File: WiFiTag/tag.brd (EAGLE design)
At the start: 46 x 36 mm, 65 parts, among them IC2 MCP73831/OT, U2 CP2104-F03-GM

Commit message: WifiTagV0.4
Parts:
- removed C4: 10uF, microbuilder:0603
- removed D2: (no value), adafruit:SOD-123
- removed EN, VBUS: (no value), wirepad:SMD1,27-2,54
- removed LED2: RED, microbuilder:CHIPLED_0603
- removed LED3: GREEN, microbuilder:CHIPLED_0603
- removed R8, R9: 10k, microbuilder:0402
- removed T1, T2: (no value), transistor:SOT23-BEC
- removed U2: CP2104-F03-GM, Silicon Labs:QFN-24-4X4
- removed U3: (no value), MicroUSB:USB-MICRO-SMD
- added GND1, SET: (no value), wirepad:SMD1,27-2,54
- added JP1, JP2: (no value), pinhead:1_05X2MM
- R4, R5: value 1k -> 10k
- moved R5 31.8 mm to (35.0, 8.00), turned to 180 degrees
- moved R4 28.4 mm to (31.0, 8.00), turned to 0 degrees
- moved C3 2.00 mm to (14.0, 18.0)
- moved C2 1.00 mm to (19.0, 27.0)
- moved C5 1.00 mm to (21.0, 27.0)
- moved R12 1.00 mm to (24.0, 29.0)
- moved U1 1.00 mm to (16.0, 27.0)
- moved R7 0.26 mm to (27.0, 8.00)
- turned R2 to 90 degrees
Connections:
- removed net D+: U2.3, U3.D+1
- removed net D-: U2.4, U3.D-1
- removed net DTR: R8.1, T2.E, U2.23
- removed net N$10: R8.2, T1.B
- removed net N$11: R9.2, T2.B
- removed net N$6: LED2.A, R4.2
- removed net N$7: LED3.A, R5.2
- removed net N$8: LED2.C, U2.14
- removed net N$9: LED3.C, U2.13
- removed net RTS: R9.1, T1.E, U2.19
- removed net VBUS: C4.1, D2.A, U2.7, U2.8, U3.VBUS1, VBUS.1
- net 0: now also JP1.1, R4.1; no longer R18.1, T2.C
- net 2: now also R18.1
- net 3.3V: now also JP2.4, R4.2, R5.2, U$24.EN
- net 5.0V: now also JP2.5; no longer D2.C
- net EN: now also JP1.5; no longer EN.1
- net GND: now also GND1.1, JP2.1; no longer C4.2, U2.2, U2.PAD, U3.GND1
- net RST: now also JP1.2, R5.1; no longer T1.C
- net RXD: now also JP1.3; no longer U2.20
- net SETLATCH: now also SET.1; no longer R4.1, R5.1, U2.5, U2.6
- net TXD: now also JP1.4; no longer U2.21
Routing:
- net DTR: track 28.5 -> 0.00 mm
- net RTS: track 28.1 -> 0.00 mm
- net 3.3V: track 62.2 -> 89.8 mm, vias 0 -> 3
- net 2: track 2.60 -> 28.2 mm, vias 0 -> 2
- net EN: track 20.0 -> 41.2 mm
- net RST: track 45.8 -> 66.0 mm
- net VBUS: track 17.4 -> 0.00 mm
- net 0: track 28.8 -> 45.1 mm, vias 2 -> 1
- net D+: track 13.0 -> 0.00 mm
- net SETLATCH: track 42.8 -> 31.3 mm, vias 5 -> 3
- net D-: track 11.5 -> 0.00 mm
- net TXD: track 44.5 -> 34.4 mm, vias 2 -> 1
- net RXD: track 45.2 -> 37.7 mm, vias 2 -> 1
- net N$10: track 4.85 -> 0.00 mm
- net 5.0V: track 40.8 -> 45.3 mm, vias 0 -> 1
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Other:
- outline, holes or cut-outs redrawn
- board text added: "V0.4"
- board text removed: "V0.3"

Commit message: new tag version 0.5
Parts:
- removed JP1, JP2: (no value), pinhead:1_05X2MM
- removed U$21, U$47, U$48, U$49: MOUNTINGHOLE2.5, microbuilder:MOUNTINGHOLE_2.5_PLATED
- removed U$24: CD4043B, masterthesis:TSSOP16
- added 16, BAT1, EN: (no value), wirepad:SMD1,27-2,54
- added Q1: (no value), microbuilder:SOT23-R
- added R8: 10k, microbuilder:0402
- R20: value 150 -> 10k
- moved SET 49.4 mm to (2.00, 3.00)
- moved GND1 41.2 mm to (4.00, 18.0)
- moved 3.3V 27.9 mm to (2.00, 27.0), turned to 90 degrees
- moved U5 23.4 mm to (33.8, 4.10), turned to 180 degrees
- moved R5 22.5 mm to (43.0, 29.0), turned to 90 degrees
- moved U4 9.09 mm to (38.0, 29.0), turned to 270 degrees
- moved 5V 9.06 mm to (2.00, 33.0), turned to 90 degrees
- moved R19 7.07 mm to (34.0, 33.0), turned to 270 degrees
- moved LED1 7.00 mm to (15.0, 33.0)
- moved LED6 7.00 mm to (15.0, 3.00)
- moved R1 7.00 mm to (13.0, 33.0)
- moved R18 7.00 mm to (13.0, 3.00), turned to 90 degrees
- moved AC1 5.00 mm to (29.0, 4.00)
- moved AC2 5.00 mm to (27.0, 4.00)
- moved BAT 5.00 mm to (27.0, 32.0)
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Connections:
- removed net BATLOW: R10.1, U$24.Q2
- removed net RESETLATCH: U$24.R1, U4.4
- removed net SETLATCH: SET.1, U$24.S1, U5.11
- new net N$6: Q1.3, R8.2, U4.2
- new net SET: Q1.2, SET.1, U5.11
- net 0: no longer JP1.1
- net 12: no longer U$24.S2
- net 14: now also R10.1; no longer U$24.R2
- net 16: now also 16.1, Q1.1; no longer U4.2
- net 2: now also LED6.C; no longer R18.1
- net 3.3V: now also R18.2, U5.8; no longer JP2.4, U$24.EN, U$24.VCC
- net 4.5V: now also BAT1.1
- net 5.0V: no longer JP2.5
- net EN: now also EN.1, U4.4; no longer JP1.5, U$24.Q1
- net GND: now also R8.1, U5.12; no longer JP2.1, LED6.C, U$24.GND
- net N$4: now also R18.1; no longer R18.2
- net RST: no longer JP1.2
- net RXD: no longer JP1.3
- net TXD: no longer JP1.4
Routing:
- net SET: track 0.00 -> 59.1 mm, vias 0 -> 2
- net 0: track 45.1 -> 2.51 mm, vias 1 -> 0
- net RST: track 66.0 -> 24.2 mm, vias 2 -> 0
- net RXD: track 37.7 -> 0.00 mm, vias 1 -> 0
- net TXD: track 34.4 -> 0.00 mm, vias 1 -> 0
- net 16: track 14.6 -> 47.0 mm
- net SETLATCH: track 31.3 -> 0.00 mm, vias 3 -> 0
- net 4.5V: track 13.2 -> 39.2 mm, vias 0 -> 2
- net 12: track 16.3 -> 0.00 mm
- net 4: track 17.9 -> 5.26 mm, vias 2 -> 0
- net 5.0V: track 45.3 -> 56.5 mm, vias 1 -> 0
- net 2: track 28.2 -> 19.0 mm
- net 3.3V: track 89.8 -> 98.2 mm, vias 3 -> 7
- net 14: track 13.0 -> 20.3 mm
- net N$6: track 0.00 -> 6.29 mm
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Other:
- outline, holes or cut-outs redrawn
- board text added: "V0.5"
- board text removed: "V0.4"

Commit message: XNOR Tag version
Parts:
- removed Q1: (no value), microbuilder:SOT23-R
- removed R8: 10k, microbuilder:0402
- removed U4: (no value), microbuilder:SOT23-5
- added C14: 470nF, microbuilder:0402
- added C4: 10nF, microbuilder:0402
- added R21, R22, R23, R9: 10k, microbuilder:0402
- added R24, R25: 100k, microbuilder:0402
- added U$46: CD4077B, masterthesis:TSSOP14
- R1: value (none) -> 1k
- moved R20 10.3 mm to (31.0, 31.5), turned to 90 degrees
- moved R19 10.3 mm to (43.0, 28.0), turned to 90 degrees
- moved R13 2.70 mm to (29.0, 28.5)
- moved U5 2.41 mm to (36.0, 5.00)
- moved R5 2.24 mm to (41.0, 28.0)
- moved R12 2.06 mm to (27.0, 28.5), turned to 90 degrees
- moved 3.3V 1.00 mm to (2.00, 28.0)
- moved C1 1.00 mm to (24.2, 32.2)
- moved D1 1.00 mm to (23.0, 29.0)
- moved IC2 1.00 mm to (21.0, 32.0)
- moved R2 1.00 mm to (18.0, 32.0)
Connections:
- removed net N$6: Q1.3, R8.2, U4.2
- new net N$10: R25.1, U$46.A
- new net N$7: R9.1, U5.7
- new net N$8: R21.2, U5.8
- new net N$9: R20.2, U$46.~G#H
- net 12: now also R11.1
- net 13: no longer R11.1
- net 16: now also U$46.B, U$46.G; no longer Q1.1
- net 3.3V: now also C14.1, C4.2, R21.1, R22.2, R23.1, R24.2, R25.2, U$46.VCC; no longer R20.1, U4.5, U5.8
- net 4: now also R22.1
- net 5: now also R23.2
- net EN: now also R20.1, R24.1, U$46.~A#B; no longer R20.2, U4.4
- net GND: now also C14.2, C4.1, R9.2, U$46.GND; no longer R8.1, U4.3
- net SET: now also U$46.H; no longer Q1.2
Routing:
- net 13: track 35.6 -> 0.00 mm
- net 12: track 0.00 -> 32.4 mm
- net RST: track 24.2 -> 6.47 mm
- net 3.3V: track 98.2 -> 113.8 mm, vias 7 -> 9
- net 16: track 47.0 -> 55.5 mm, vias 2 -> 4
- net EN: track 47.5 -> 54.1 mm, vias 2 -> 6
- net N$6: track 6.29 -> 0.00 mm
- net N$10: track 0.00 -> 5.00 mm, vias 0 -> 2
- net SET: track 59.1 -> 63.9 mm
- net N$7: track 0.00 -> 4.59 mm, vias 0 -> 2
- net N$9: track 0.00 -> 3.90 mm
- net 14: track 20.3 -> 23.0 mm, vias 0 -> 2
- net 5: track 13.1 -> 15.7 mm
- net 4: track 5.26 -> 7.55 mm
- net 5.0V: track 56.5 -> 58.4 mm
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
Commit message: XNOR Tag version
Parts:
- removed AC1, AC2, BAT1, GND1: (no value), wirepad:SMD1,27-2,54
- removed C14: 470nF, microbuilder:0402
- removed C4: 10nF, microbuilder:0402
- removed R21, R22, R9: 10k, microbuilder:0402
- removed U5: (no value), microbuilder:LGA16_3X3MM
- added C17: 1uF, microbuilder:0402
- added C18: 100nf, microbuilder:0402
- added JP1, JP2: (no value), microbuilder:1X02_OVAL
- added Q3, Q4: BSS138, microbuilder:SOT23-WIDE
- added R31, R33, R34, R35, R36: 10K, microbuilder:0402
- added U3: LIS3DHTR, microbuilder:LGA16_3X3MM
- R32: value 10k -> 10K
- moved R11 32.2 mm to (17.0, 22.0)
- moved GND 28.7 mm to (4.00, 18.0), turned to 90 degrees
- moved BAT 26.9 mm to (2.00, 22.0), turned to 90 degrees
- moved R7 16.6 mm to (20.0, 23.0)
- moved R6 13.6 mm to (20.0, 21.0)
- moved R4 2.00 mm to (28.0, 8.00), turned to 180 degrees
- moved C3 1.00 mm to (14.0, 22.0)
- moved R3 1.00 mm to (14.0, 24.0)
- moved U1 1.00 mm to (14.0, 27.0)
- turned R32 to 270 degrees
- renumbered R23 to R32
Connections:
- removed net 4: R22.1, U5.6, X1.14
- removed net 5: R32.2, U5.4, X1.13
- removed net N$7: R9.1, U5.7
- removed net N$8: R21.2, U5.8
- new net ADC1: U3.16
- new net ADC2: U3.15
- new net ADC3: U3.13
- new net N$11: R31.1, U3.8
- new net SCL: Q4.3, R35.1, X1.13
- new net SCL_3.3V: Q4.2, R33.1, U3.4
- new net SDA: Q3.3, R34.1, X1.14
- new net SDA_3.3V: Q3.2, R32.1, U3.6
- new net SDO: R36.2, U3.7
- net 3.3V: now also C17.1, C18.1, Q3.1, Q4.1, R31.2, R32.2, R33.2, R34.2, R35.2, U3.1, U3.14; no longer C14.1, C4.2, R21.1, R22.2, R32.1, U5.1, U5.14
- net 4.5V: now also JP1.1; no longer BAT1.1
- net AC1: now also JP2.1; no longer AC1.1
- net AC2: now also JP2.2; no longer AC2.1
- net GND: now also C17.2, C18.2, JP1.2, R36.1, U3.10, U3.12, U3.5; no longer C14.2, C4.1, GND1.1, R9.2, U5.10, U5.12, U5.5
- net SET: now also U3.11; no longer U5.11
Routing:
- net N$13: track 2.04 -> 43.5 mm, vias 0 -> 2
- net 12: track 32.4 -> 12.3 mm, vias 0 -> 2
- net 5: track 15.7 -> 0.00 mm
- net 2: track 19.0 -> 32.3 mm
- net SDA_3.3V: track 0.00 -> 11.1 mm, vias 0 -> 2
- net SET: track 63.9 -> 74.5 mm, vias 2 -> 3
- net SDA: track 0.00 -> 10.0 mm
- net SDO: track 0.00 -> 8.15 mm
- net 4: track 7.55 -> 0.00 mm
- net SCL_3.3V: track 0.00 -> 7.54 mm, vias 0 -> 2
- net SCL: track 0.00 -> 6.43 mm
- net N$11: track 0.00 -> 5.53 mm
- net N$7: track 4.59 -> 0.00 mm, vias 2 -> 0
- net 3.3V: track 113.8 -> 117.6 mm, vias 9 -> 6
- net N$10: track 5.00 -> 7.50 mm
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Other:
- board text added: "V0.6"
- board text removed: "V0.5"

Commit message: V06 of PCB
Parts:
- removed R20: 10k, microbuilder:0402
- removed R25: 100k, microbuilder:0402
- removed U$46: CD4077B, masterthesis:TSSOP14
- added U2: (no value), microbuilder:SOT23-5
- R24: value 100k -> 10k
- moved R19 12.0 mm to (31.0, 28.5), turned to 270 degrees
- moved R5 6.02 mm to (35.0, 28.5)
- moved R24 2.00 mm to (33.0, 28.5), turned to 90 degrees
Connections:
- removed net N$10: R25.1, U$46.A
- removed net N$9: R20.2, U$46.~G#H
- net 16: no longer U$46.B, U$46.G
- net 3.3V: now also U2.5; no longer R25.2, U$46.VCC
- net EN: no longer R20.1, U$46.~A#B
- net GND: now also U2.3; no longer U$46.GND
- net RST: now also U2.4
- net SET: now also U2.2; no longer U$46.H
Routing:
- net EN: track 54.4 -> 41.4 mm, vias 6 -> 2
- net 16: track 55.5 -> 42.6 mm, vias 4 -> 2
- net N$10: track 7.50 -> 0.00 mm, vias 2 -> 0
- net RST: track 6.47 -> 13.0 mm
- net N$9: track 3.90 -> 0.00 mm
- net 3.3V: track 117.6 -> 116.4 mm, vias 6 -> 4

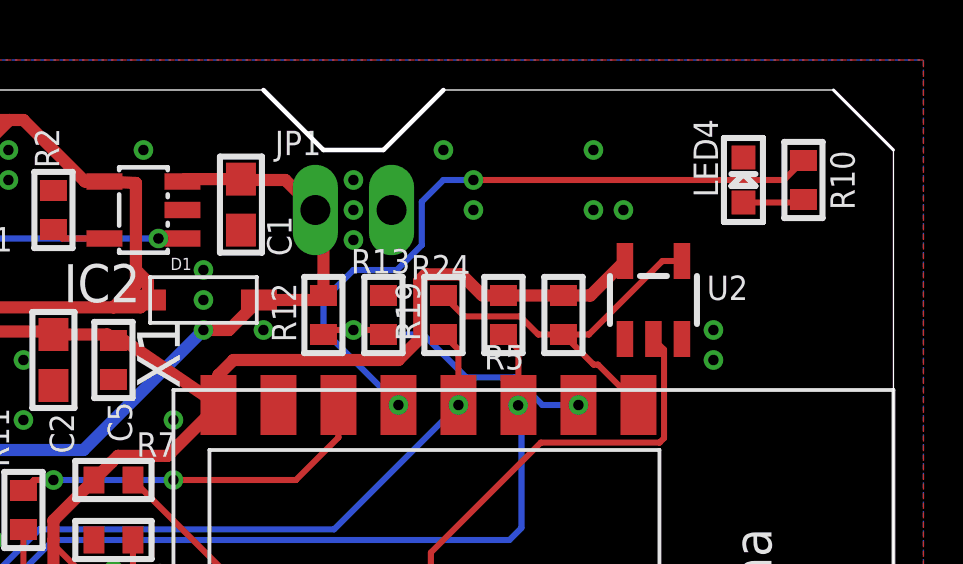
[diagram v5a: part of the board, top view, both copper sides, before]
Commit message: Saving current wifitag state
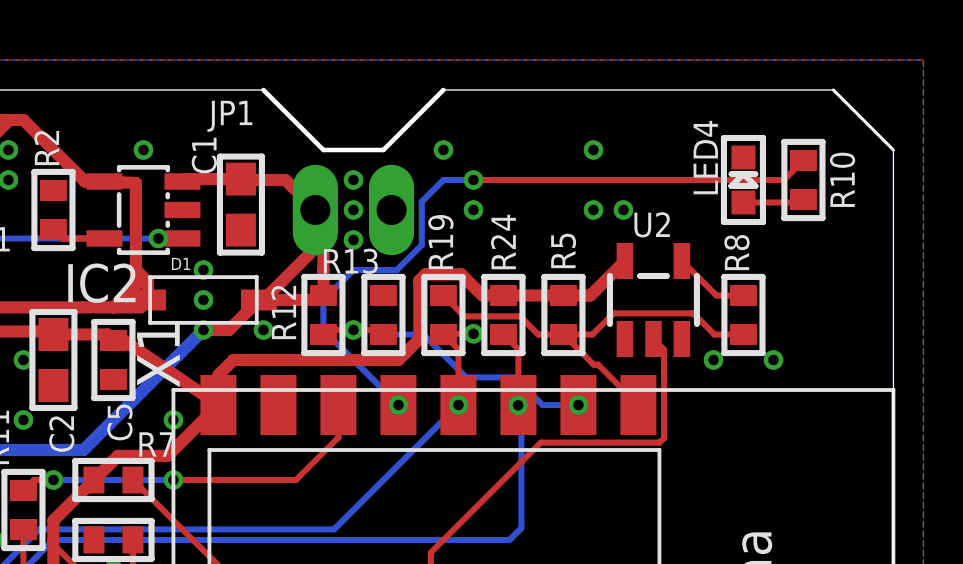
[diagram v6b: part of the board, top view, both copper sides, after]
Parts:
- added R8: 150, microbuilder:0402
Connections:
- new net N$6: R8.2, U2.4
- net RST: now also R8.1; no longer U2.4
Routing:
- net 4.5V: track 36.2 -> 39.9 mm
- net N$6: track 0.00 -> 2.53 mm
- net RST: track 13.0 -> 14.6 mm
- net 16: track 42.6 -> 43.6 mm, vias 2 -> 3
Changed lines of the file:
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@@
 </element>
 <element name="C1" library="microbuilder" package="0603" value="10uF" x="24.25" y="32.18" smashed="yes" rot="R270">
-<attribute name="NAME" x="25.123" y="31.802" size="0.8128" layer="25" font="vector" ratio="18" rot="R270"/>
+<attribute name="NAME" x="22.623" y="34.502" size="0.8128" layer="25" font="vector" ratio="18" rot="R270"/>
 <attribute name="VALUE" x="25.288" y="33.202" size="0.4064" layer="27" font="vector" ratio="10" rot="R270"/>
 </element>
@@
 </element>
 <element name="R13" library="microbuilder" package="0402" value="500k" x="29" y="28.5" smashed="yes" rot="R90">
-<attribute name="NAME" x="29.8905" y="30.697" size="0.8128" layer="25" ratio="18" rot="R180"/>
+<attribute name="NAME" x="28.8905" y="30.697" size="0.8128" layer="25" ratio="18" rot="R180"/>
 <attribute name="VALUE" x="29.435" y="25.597" size="0.4064" layer="27" ratio="10" rot="R180"/>
 </element>
@@
 </element>
 <element name="R19" library="microbuilder" package="0402" value="150" x="31" y="28.5" smashed="yes" rot="R270">
-<attribute name="NAME" x="29.4095" y="29.603" size="0.8128" layer="25" ratio="18" rot="R270"/>
+<attribute name="NAME" x="30.5095" y="31.903" size="0.8128" layer="25" ratio="18" rot="R270"/>
 <attribute name="VALUE" x="31.765" y="28.203" size="0.4064" layer="27" ratio="10" rot="R270"/>
 </element>
@@
 </element>
 <element name="R5" library="microbuilder" package="0402" value="10k" x="35" y="28.5" smashed="yes" rot="R90">
-<attribute name="NAME" x="33.6905" y="27.497" size="0.8128" layer="25" ratio="18" rot="R180"/>
+<attribute name="NAME" x="34.5905" y="31.297" size="0.8128" layer="25" ratio="18" rot="R270"/>
 <attribute name="VALUE" x="35.635" y="27.097" size="0.4064" layer="27" ratio="10" rot="R180"/>
 </element>
@@
 <element name="EN" library="wirepad" library_urn="urn:adsk.eagle:library:412" package="SMD1,27-2,54" package3d_urn="urn:adsk.eagle:package:30839/1" value="" x="2" y="14" rot="R90"/>
 <element name="R24" library="microbuilder" package="0402" value="10k" x="33" y="28.5" smashed="yes" rot="R90">
-<attribute name="NAME" x="31.8905" y="30.497" size="0.8128" layer="25" ratio="18" rot="R180"/>
+<attribute name="NAME" x="32.6" y="31.9" size="0.8128" layer="25" ratio="18" rot="R270"/>
 <attribute name="VALUE" x="34.135" y="27.497" size="0.4064" layer="27" ratio="10" rot="R90"/>
 </element>
@@
 <attribute name="VALUE" x="35.865" y="3.603" size="0.4064" layer="27" ratio="10" rot="R270"/>
 </element>
-<element name="JP1" library="microbuilder" package="1X02_OVAL" value="" x="28" y="32"/>
+<element name="JP1" library="microbuilder" package="1X02_OVAL" value="" x="28" y="32" smashed="yes">
+<attribute name="NAME" x="23.1838" y="34.8288" size="0.8128" layer="25" ratio="18"/>
+<attribute name="VALUE" x="25.46" y="28.825" size="0.4064" layer="27" ratio="10"/>
+</element>
 <element name="JP2" library="microbuilder" package="1X02_OVAL" value="" x="28" y="4" smashed="yes" rot="R180">
 <attribute name="NAME" x="32.7162" y="1.3712" size="0.8128" layer="25" ratio="18" rot="R180"/>
 <attribute name="VALUE" x="30.54" y="7.175" size="0.4064" layer="27" ratio="10" rot="R180"/>
 </element>
-<element name="U2" library="microbuilder" package="SOT23-5" value="" x="38" y="29"/>
+<element name="U2" library="microbuilder" package="SOT23-5" value="" x="38" y="29" smashed="yes">
+<attribute name="NAME" x="37.278" y="31.1" size="0.8128" layer="25" ratio="18"/>
+<attribute name="VALUE" x="39.778" y="28.365" size="0.4064" layer="27" ratio="10"/>
+</element>
+<element name="R8" library="microbuilder" package="0402" value="150" x="41" y="28.5" rot="R90"/>
 </elements>
 <signals>
@@
 <wire x1="25" y1="29" x2="24.85" y2="29" width="0.2032" layer="1"/>
 <wire x1="26.73" y1="32" x2="27" y2="31.73" width="0.4064" layer="1"/>
-<wire x1="27" y1="31.73" x2="27" y2="29.15" width="0.4064" layer="1"/>
+<wire x1="27" y1="31.73" x2="27" y2="30" width="0.4064" layer="1"/>
+<wire x1="27" y1="30" x2="27" y2="29.15" width="0.4064" layer="1"/>
 <wire x1="27" y1="29.15" x2="26.85" y2="29" width="0.4064" layer="1"/>
 <wire x1="26.85" y1="29" x2="25" y2="29" width="0.4064" layer="1"/>
 <wire x1="26.73" y1="32" x2="25.73" y2="33" width="0.4064" layer="1"/>
 <wire x1="25.73" y1="33" x2="24.28" y2="33" width="0.4064" layer="1"/>
+<wire x1="26.73" y1="32" x2="26.73" y2="30.73" width="0.4064" layer="1"/>
+<wire x1="26.73" y1="30.73" x2="25" y2="29" width="0.4064" layer="1"/>
 </signal>
 <signal name="N$3">
@@
 <via x="28" y="33" extent="1-16" drill="0.35"/>
 <via x="28" y="32" extent="1-16" drill="0.35"/>
-<via x="40" y="28" extent="1-16" drill="0.35"/>
+<via x="42" y="27" extent="1-16" drill="0.35"/>
 <via x="36" y="34" extent="1-16" drill="0.35"/>
 <via x="17" y="27" extent="1-16" drill="0.35"/>
@@
 <contactref element="R19" pad="1"/>
 <contactref element="R5" pad="1"/>
-<contactref element="U2" pad="4"/>
 <wire x1="31" y1="29.15" x2="31.696" y2="28.454" width="0.2032" layer="1"/>
 <wire x1="34.1592125" y1="27.85" x2="35" y2="27.85" width="0.2032" layer="1"/>
 <wire x1="31.696" y1="28.454" x2="33.5552125" y2="28.454" width="0.2032" layer="1"/>
 <wire x1="33.5552125" y1="28.454" x2="34.1592125" y2="27.85" width="0.2032" layer="1"/>
-<wire x1="35" y1="27.85" x2="35.85" y2="27.85" width="0.2032" layer="1"/>
-<wire x1="38.3001" y1="30.3001" x2="38.95" y2="30.3001" width="0.2032" layer="1"/>
-<wire x1="35.85" y1="27.85" x2="38.3001" y2="30.3001" width="0.2032" layer="1"/>
 <wire x1="35" y1="27.85" x2="36.0041" y2="26.8459" width="0.2032" layer="1"/>
 <wire x1="36.0041" y1="26.8459" x2="36.1541" y2="26.8459" width="0.2032" layer="1"/>
 <wire x1="36.1541" y1="26.8459" x2="37.5" y2="25.5" width="0.2032" layer="1"/>
+<contactref element="R8" pad="1"/>
+<wire x1="41" y1="27.85" x2="40.0341125" y2="27.85" width="0.2032" layer="1"/>
+<wire x1="35.9658875" y1="27.85" x2="35" y2="27.85" width="0.2032" layer="1"/>
+<wire x1="40.0341125" y1="27.85" x2="39.3302125" y2="28.5539" width="0.2032" layer="1"/>
+<wire x1="39.3302125" y1="28.5539" x2="36.6697875" y2="28.5539" width="0.2032" layer="1"/>
+<wire x1="36.6697875" y1="28.5539" x2="35.9658875" y2="27.85" width="0.2032" layer="1"/>
 </signal>
 <signal name="ADC">
@@
 <wire x1="31.5" y1="25.5" x2="31.5" y2="27.35" width="0.2032" layer="1"/>
 <wire x1="31.5" y1="27.35" x2="31" y2="27.85" width="0.2032" layer="1"/>
+<wire x1="31" y1="27.85" x2="31.0226" y2="27.8726" width="0.2032" layer="1"/>
+<wire x1="31.0226" y1="27.8726" x2="32" y2="27.8726" width="0.2032" layer="1"/>
+<via x="32" y="27.8726" extent="1-16" drill="0.35"/>
 </signal>
 <signal name="14">
@@
 <contactref element="U3" pad="13"/>
 </signal>
+<signal name="N$6">
+<contactref element="U2" pad="4"/>
+<contactref element="R8" pad="2"/>
+<wire x1="38.95" y1="30.3001" x2="40.1001" y2="29.15" width="0.2032" layer="1"/>
+<wire x1="40.1001" y1="29.15" x2="41" y2="29.15" width="0.2032" layer="1"/>
+</signal>
 </signals>
